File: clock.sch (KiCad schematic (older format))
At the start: 24 parts, among them IC41 74LS175, IC42 8284, IC55 74LS107, IC71 74LS74, Q2 2N3904

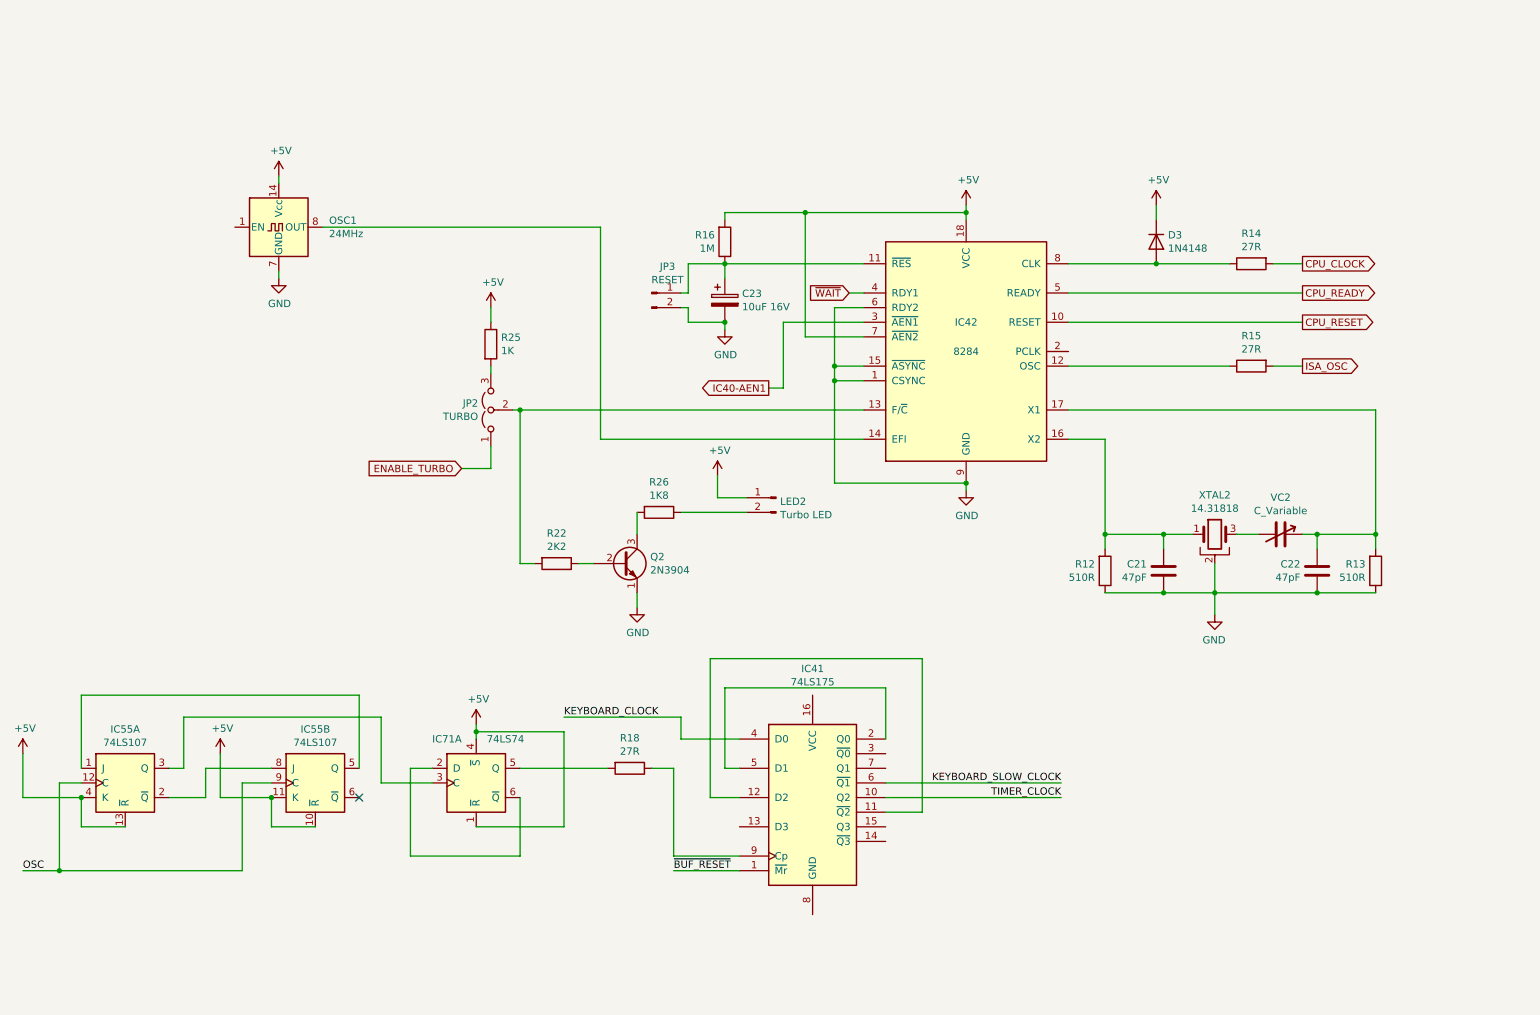
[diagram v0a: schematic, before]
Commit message: Tidy up and map all signals
This fixes up the schematic to:
 - Look presentable
 - Fix all labels connecting sheets
 - Tidy up all loose ends by either inspecting the PCB under
    magnification, measuring with an oscillosope or buzzing
    out with a meter
 - Pass ERC (with 1 exception due to incorrect circuitry around
    pin 33 on the FPU (~RQ~/~GT1~)
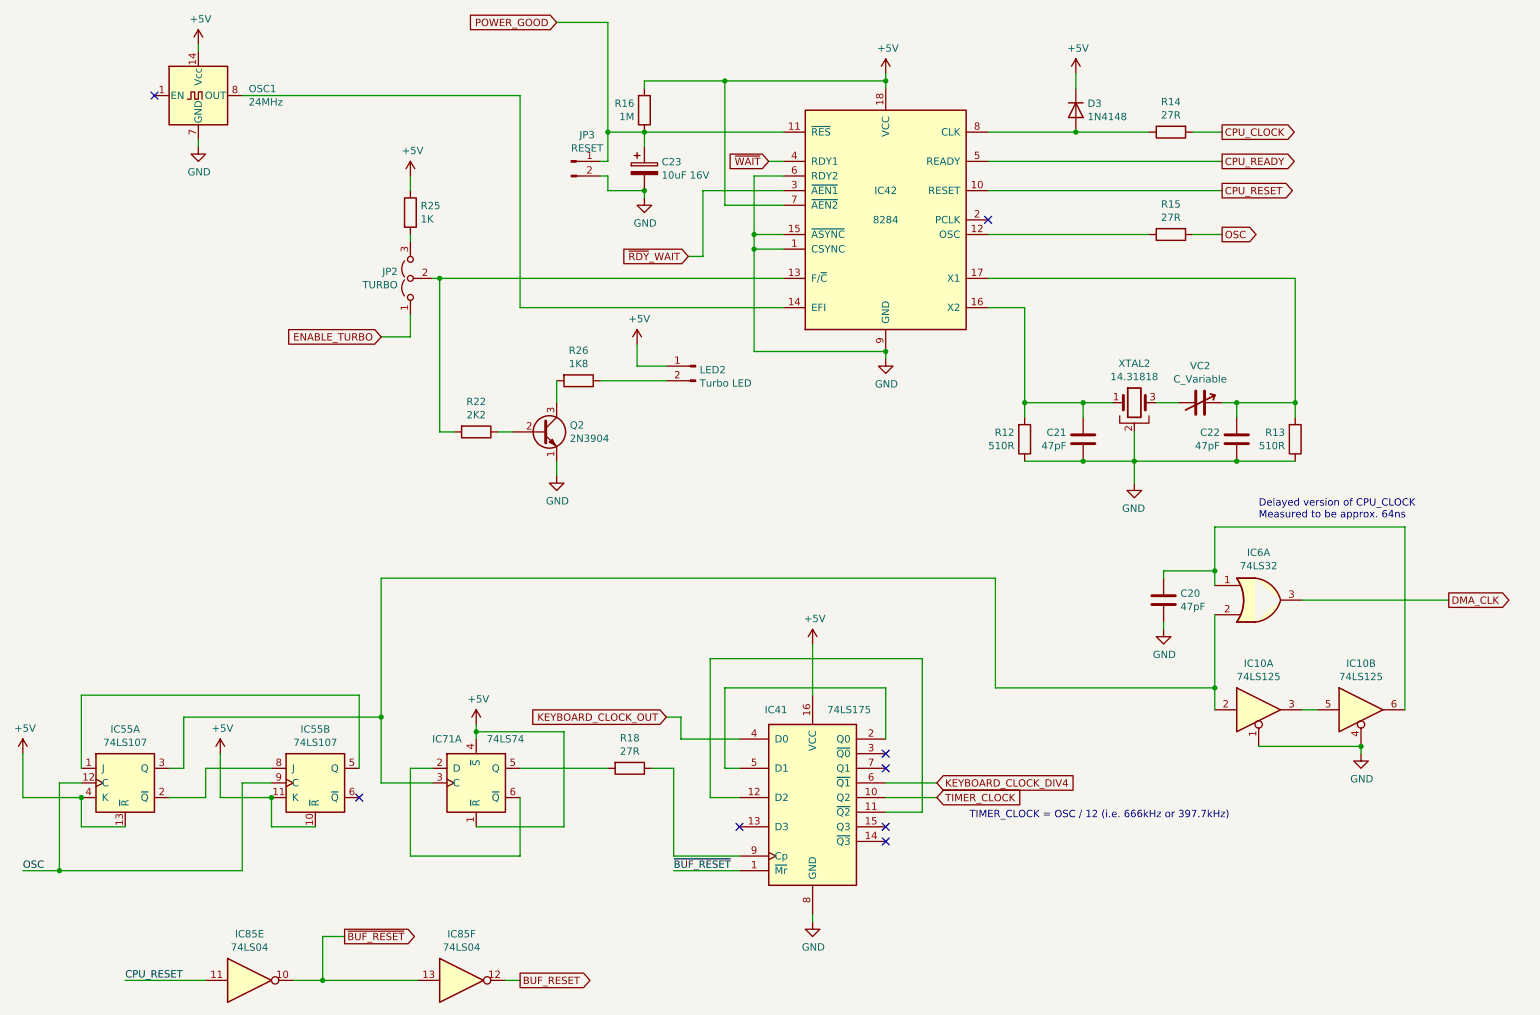
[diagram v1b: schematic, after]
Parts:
- added C20: 47pF, symbol Device:C
- added IC10: 74LS125, symbol 74xx:74LS125
- added IC6: 74LS32, symbol 74xx:74LS32
- added IC85: 74LS04, symbol 74xx:74LS04
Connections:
- net ISA_OSC is gone; now on net OSC: R15.2
- net +5V: now also IC41.16 (VCC)
- net CPU_RESET: now also IC85.11
- net GND: now also IC41.8 (GND), C20.2, IC10.1, IC10.4
- net ~BUF_RESET~: now also IC85.10, IC85.13
- net POWER_GOOD: now reaches C23.1, IC42.11 (~RES~), JP3.1 (Pin_1), R16.1
- net at IC55.3 (Q), IC71.3 (C): now also IC10.2, IC6.2
- net IC40-AEN1 renamed ~RDY~_WAIT
- net KEYBOARD_CLOCK renamed KEYBOARD_CLOCK_OUT
- net KEYBOARD_SLOW_CLOCK renamed KEYBOARD_CLOCK_DIV4
- new net: IC10.3, IC10.5
- new net: C20.1, IC10.6, IC6.1
- new net BUF_RESET: IC85.12
- new net DMA_CLK: IC6.3
- no-connect marks 1 -> 8
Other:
- note added: "Delayed version of CPU_CLOCK\nMeasured to be approx. 64ns"
- note added: "TIMER_CLOCK = OSC / 12 (i.e. 666kHz or 397.7kHz)"
- moved on the sheet: C21, C22, C23, D3, IC42, JP2, JP3, LED2, OSC1, Q2, R12, R13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

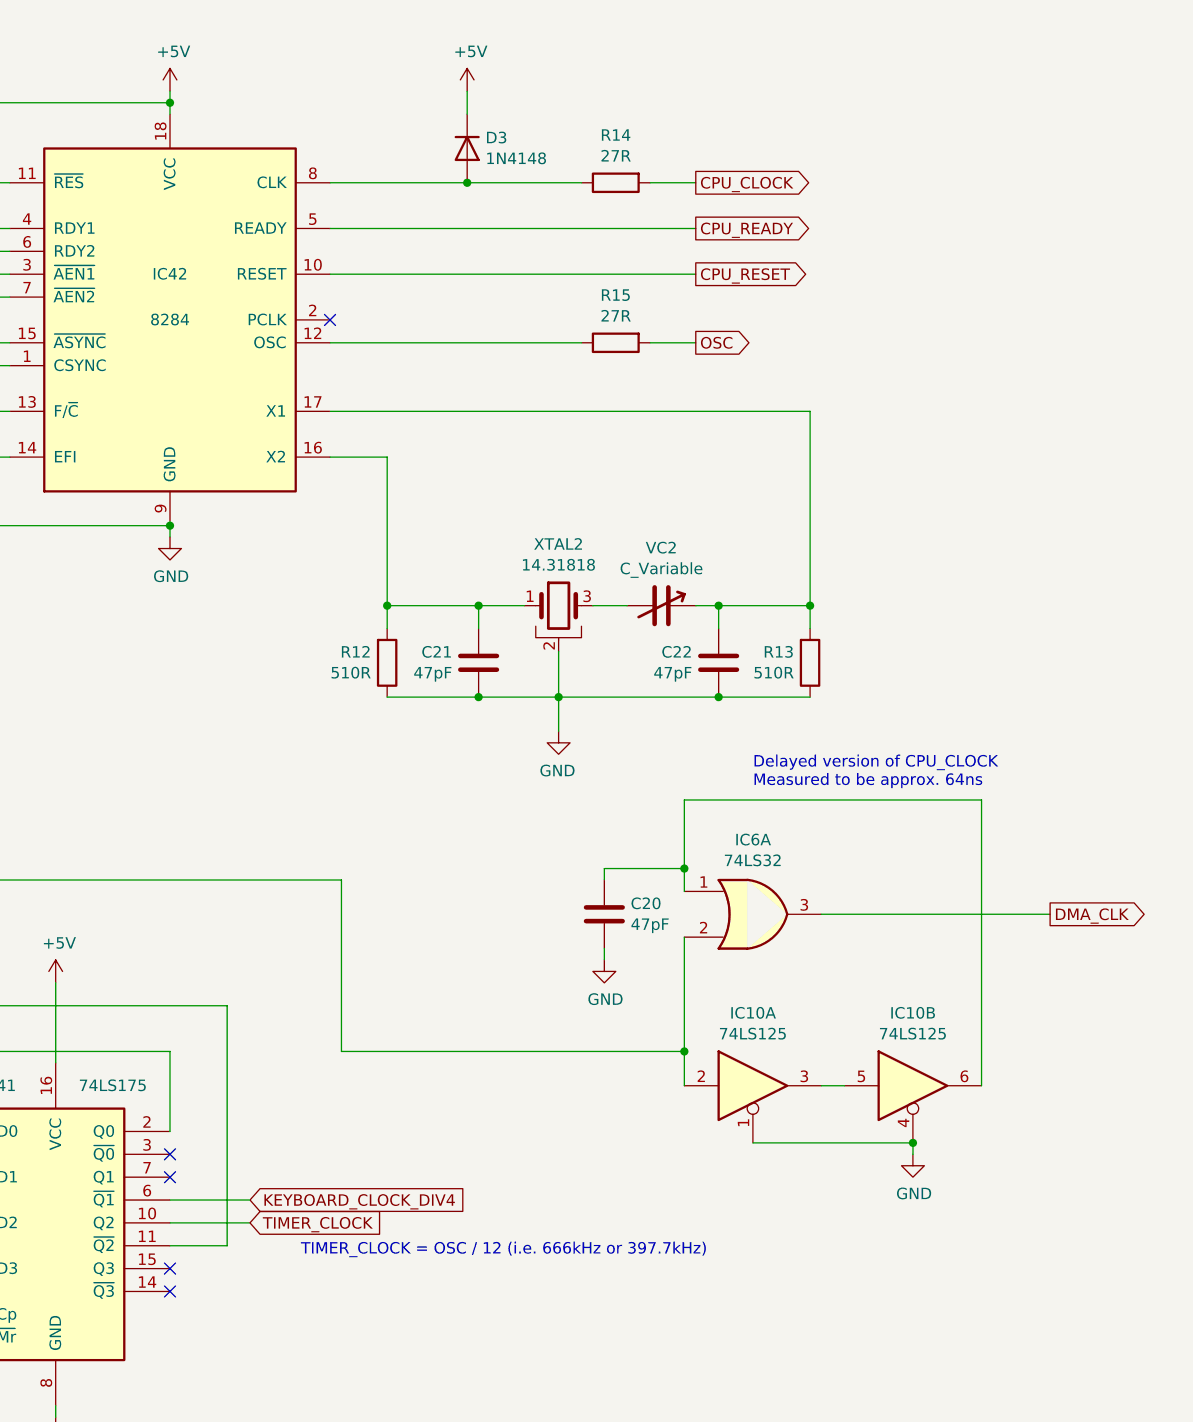
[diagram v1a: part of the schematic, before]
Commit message: Fix clock frequencies
This fixes the notes describing the clock frequencies having
properly computed what they should be.
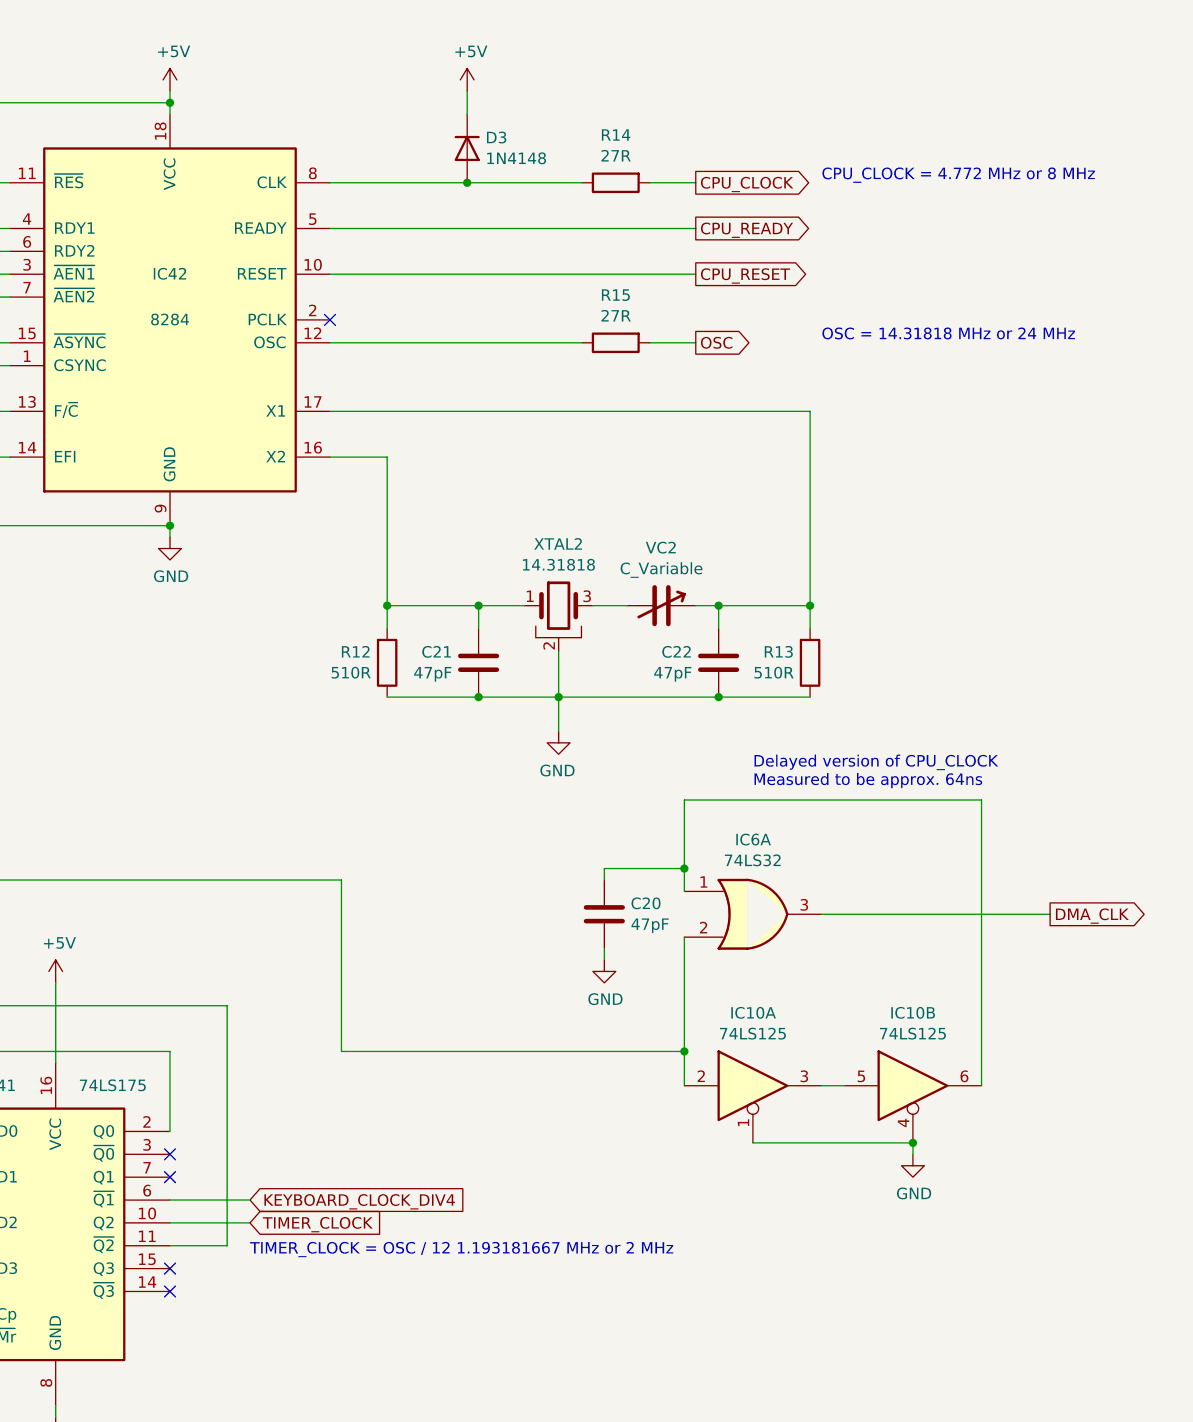
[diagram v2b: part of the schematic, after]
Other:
- note added: "CPU_CLOCK = 4.772 MHz or 8 MHz"
- note added: "OSC = 14.31818 MHz or 24 MHz"
- note added: "TIMER_CLOCK = OSC / 12 1.193181667 MHz or 2 MHz"
- note removed: "TIMER_CLOCK = OSC / 12 (i.e. 666kHz or 397.7kHz)"
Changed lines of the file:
@@
 Text Label 5050 6600 0    50   ~ 0
 ~BUF_RESET~
-Text Notes 8850 6250 2    50   ~ 0
-TIMER_CLOCK = OSC / 12 (i.e. 666kHz or 397.7kHz)
+Text Notes 6850 6250 0    50   ~ 0
+TIMER_CLOCK = OSC / 12 1.193181667 MHz or 2 MHz
 Text GLabel 4250 800  0    50   Input ~ 0
 POWER_GOOD
@@
 Text Notes 9050 4200 0    50   ~ 0
 Delayed version of CPU_CLOCK\nMeasured to be approx. 64ns
+Text Notes 9350 1550 0    50   ~ 0
+CPU_CLOCK = 4.772 MHz or 8 MHz
+Text Notes 9350 2250 0    50   ~ 0
+OSC = 14.31818 MHz or 24 MHz
 $EndSCHEMATC
